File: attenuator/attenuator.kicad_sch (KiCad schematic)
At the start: 25 parts, among them J1 Conn_Coaxial, J11 Conn_02x07_Odd_Even, J2 Conn_Coaxial

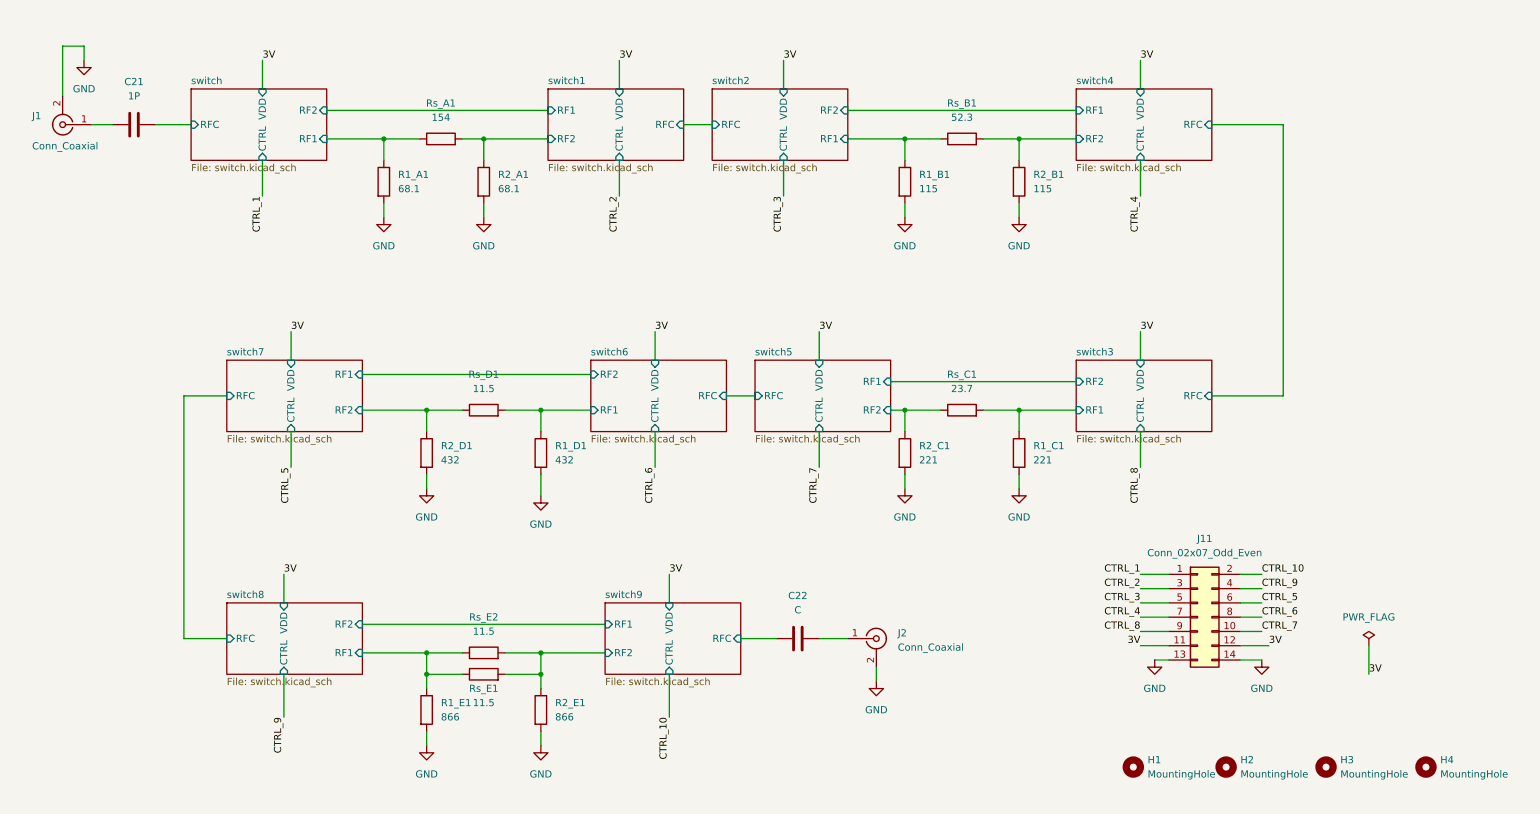
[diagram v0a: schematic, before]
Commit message: change hierarchical sheets
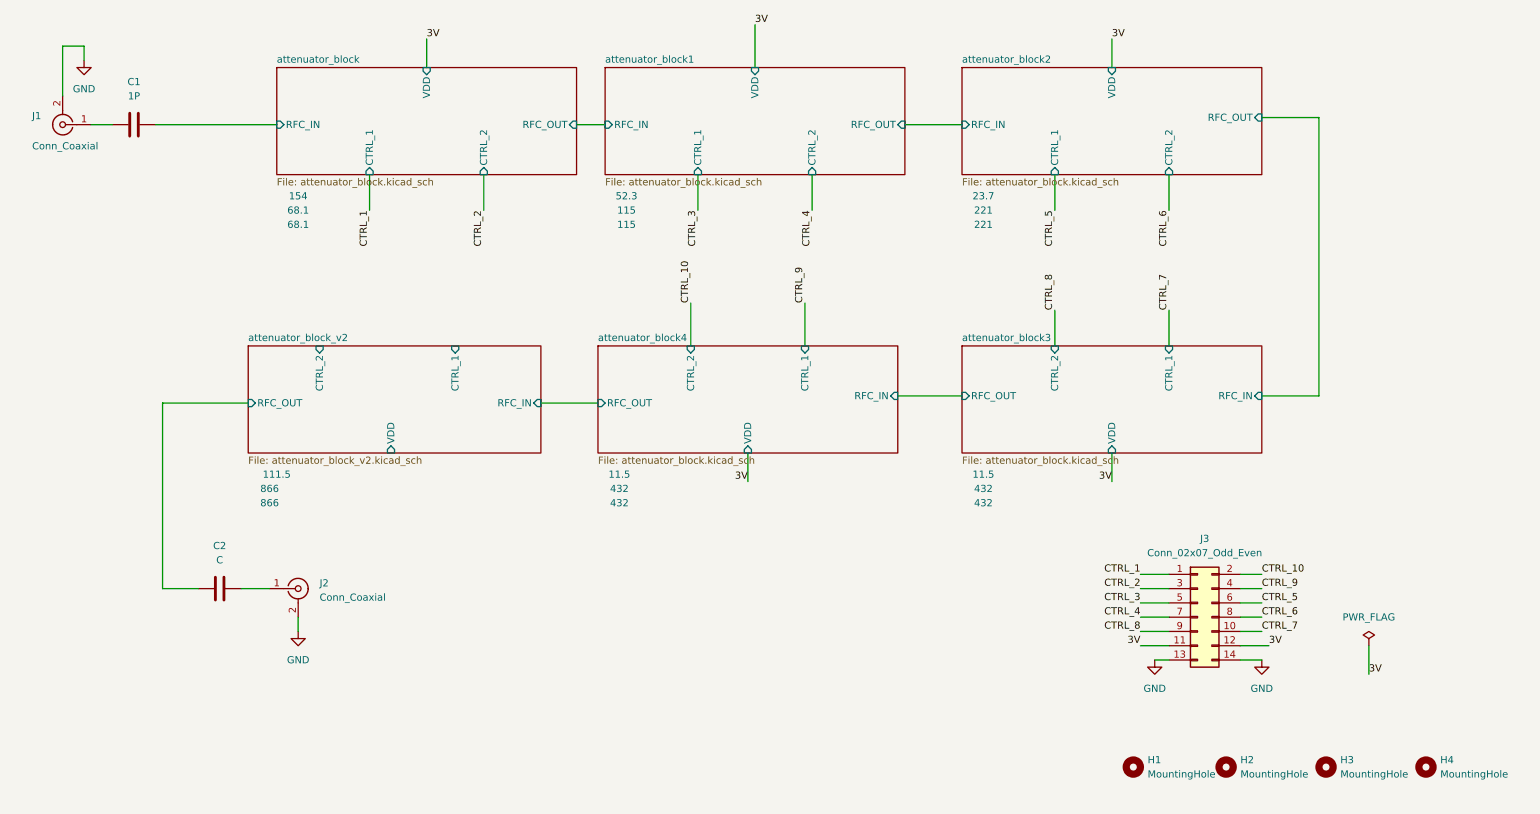
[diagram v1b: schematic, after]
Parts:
- removed R1_A1, R2_A1: 68.1, Resistor_SMD:R_0805_2012Metric_Pad1.20x1.40mm_HandSolder, symbol Device:R
- removed R1_B1, R2_B1: 115, Resistor_SMD:R_0805_2012Metric_Pad1.20x1.40mm_HandSolder, symbol Device:R
- removed R1_C1, R2_C1: 221, Resistor_SMD:R_0805_2012Metric_Pad1.20x1.40mm_HandSolder, symbol Device:R
- removed R1_D1, R2_D1: 432, Resistor_SMD:R_0805_2012Metric_Pad1.20x1.40mm_HandSolder, symbol Device:R
- removed R1_E1, R2_E1: 866, Resistor_SMD:R_0805_2012Metric_Pad1.20x1.40mm_HandSolder, symbol Device:R
- removed Rs_A1: 154, Resistor_SMD:R_0805_2012Metric_Pad1.20x1.40mm_HandSolder, symbol Device:R
- removed Rs_B1: 52.3, Resistor_SMD:R_0805_2012Metric_Pad1.20x1.40mm_HandSolder, symbol Device:R
- removed Rs_C1: 23.7, Resistor_SMD:R_0805_2012Metric_Pad1.20x1.40mm_HandSolder, symbol Device:R
- removed Rs_D1, Rs_E1, Rs_E2: 11.5, Resistor_SMD:R_0805_2012Metric_Pad1.20x1.40mm_HandSolder, symbol Device:R
- renumbered C21 to C1, C22 to C2, J11 to J3
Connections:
- net switch/RFC renamed attenuator_block/RFC_IN
- net switch9/RFC renamed attenuator_block_v2/RFC_OUT
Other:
- removed sheet switch
- removed sheet switch1
- removed sheet switch2
- removed sheet switch3
- removed sheet switch4
- removed sheet switch5
- removed sheet switch6
- removed sheet switch7
- removed sheet switch8
- removed sheet switch9
- added sheet attenuator_block (attenuator_block.kicad_sch)
- added sheet attenuator_block1 (attenuator_block.kicad_sch)
- added sheet attenuator_block2 (attenuator_block.kicad_sch)
- added sheet attenuator_block3 (attenuator_block.kicad_sch)
- added sheet attenuator_block4 (attenuator_block.kicad_sch)
- added sheet attenuator_block_v2 (attenuator_block_v2.kicad_sch)
- moved on the sheet: C2, J2

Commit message: pcb improve it
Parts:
- C1, C2: footprint Capacitor_SMD:C_0805_2012Metric -> Capacitor_SMD:C_0603_1608Metric
- J3: footprint Connector_PinHeader_2.54mm:PinHeader_2x07_P2.54mm_Vertical -> Connector_PinSocket_1.27mm:PinSocket_2x07_P1.27mm_Vertical
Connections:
- net CTRL_1: now also J3.9 (Pin_9); no longer J3.1 (Pin_1)
- net CTRL_10: now also J3.10 (Pin_10); no longer J3.2 (Pin_2)
- net CTRL_2: now also J3.7 (Pin_7); no longer J3.3 (Pin_3)
- net CTRL_4: now also J3.3 (Pin_3); no longer J3.7 (Pin_7)
- net CTRL_5: now also J3.1 (Pin_1); no longer J3.6 (Pin_6)
- net CTRL_6: now also J3.2 (Pin_2); no longer J3.8 (Pin_8)
- net CTRL_7: now also J3.4 (Pin_4); no longer J3.10 (Pin_10)
- net CTRL_8: now also J3.6 (Pin_6); no longer J3.9 (Pin_9)
- net CTRL_9: now also J3.8 (Pin_8); no longer J3.4 (Pin_4)
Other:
- removed sheet attenuator_block4
- moved on the sheet: C2, J2

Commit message: minnor changes in pcb
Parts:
- removed H1, H2, H3, H4: MountingHole, MountingHole:MountingHole_3.2mm_M3_Pad_TopBottom, symbol Mechanical:MountingHole
- added H5, H6, H7, H8: MountingHole_Pad, MountingHole:MountingHole_3.2mm_M3_Pad_TopBottom, symbol Mechanical:MountingHole_Pad
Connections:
- net GND: now also H5.1, H6.1, H7.1, H8.1
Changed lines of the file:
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@@
-    )
-  )
-  (symbol (lib_id "Mechanical:MountingHole") (at 264.16 157.48 0) (unit 1)
-    (in_bom yes) (on_board yes) (dnp no) (fields_autoplaced)
-    (property "Reference" "H4" (at 266.7 156.21 0)
-      (effects (font (size 1.27 1.27)) (justify left))
-    )
-    (property "Value" "MountingHole" (at 266.7 158.75 0)
-      (effects (font (size 1.27 1.27)) (justify left))
-    )
-    (property "Footprint" "MountingHole:MountingHole_3.2mm_M3_Pad_TopBottom" (at 264.16 157.48 0)
-      (effects (font (size 1.27 1.27)) hide)
-    )
-    (property "Datasheet" "~" (at 264.16 157.48 0)
-      (effects (font (size 1.27 1.27)) hide)
-    )
-    (instances
-      (project "attenuator"
-        (path "/3b0f5433-415e-45c9-9c4a-85a692e565e5"
-          (reference "H4") (unit 1)
-        )
-      )
     )
   )
@@
     )
   )
-  (symbol (lib_id "Mechanical:MountingHole") (at 246.38 157.48 0) (unit 1)
-    (in_bom yes) (on_board yes) (dnp no) (fields_autoplaced)
-    (property "Reference" "H3" (at 248.92 156.21 0)
-      (effects (font (size 1.27 1.27)) (justify left))
-    )
-    (property "Value" "MountingHole" (at 248.92 158.75 0)
-      (effects (font (size 1.27 1.27)) (justify left))
-    )
-    (property "Footprint" "MountingHole:MountingHole_3.2mm_M3_Pad_TopBottom" (at 246.38 157.48 0)
-      (effects (font (size 1.27 1.27)) hide)
-    )
-    (property "Datasheet" "~" (at 246.38 157.48 0)
-      (effects (font (size 1.27 1.27)) hide)
-    )
-    (instances
-      (project "attenuator"
-        (path "/3b0f5433-415e-45c9-9c4a-85a692e565e5"
-          (reference "H3") (unit 1)
-        )
-      )
-    )
-  )
   (symbol (lib_id "power:GND") (at 234.95 138.43 0) (unit 1)
     (in_bom yes) (on_board yes) (dnp no) (fields_autoplaced)
@@
         (path "/3b0f5433-415e-45c9-9c4a-85a692e565e5"
           (reference "#PWR03") (unit 1)
-        )
-      )
-    )
-  )
-  (symbol (lib_id "Mechanical:MountingHole") (at 212.09 157.48 0) (unit 1)
-    (in_bom yes) (on_board yes) (dnp no) (fields_autoplaced)
-    (property "Reference" "H1" (at 214.63 156.21 0)
-      (effects (font (size 1.27 1.27)) (justify left))
-    )
-    (property "Value" "MountingHole" (at 214.63 158.75 0)
-      (effects (font (size 1.27 1.27)) (justify left))
-    )
-    (property "Footprint" "MountingHole:MountingHole_3.2mm_M3_Pad_TopBottom" (at 212.09 157.48 0)
-      (effects (font (size 1.27 1.27)) hide)
-    )
-    (property "Datasheet" "~" (at 212.09 157.48 0)
-      (effects (font (size 1.27 1.27)) hide)
-    )
-    (instances
-      (project "attenuator"
-        (path "/3b0f5433-415e-45c9-9c4a-85a692e565e5"
-          (reference "H1") (unit 1)
         )
       )
@@
     )
   )
-  (symbol (lib_id "Mechanical:MountingHole") (at 228.6 157.48 0) (unit 1)
-    (in_bom yes) (on_board yes) (dnp no) (fields_autoplaced)
-    (property "Reference" "H2" (at 231.14 156.21 0)
-      (effects (font (size 1.27 1.27)) (justify left))
-    )
-    (property "Value" "MountingHole" (at 231.14 158.75 0)
-      (effects (font (size 1.27 1.27)) (justify left))
-    )
-    (property "Footprint" "MountingHole:MountingHole_3.2mm_M3_Pad_TopBottom" (at 228.6 157.48 0)
-      (effects (font (size 1.27 1.27)) hide)
-    )
-    (property "Datasheet" "~" (at 228.6 157.48 0)
-      (effects (font (size 1.27 1.27)) hide)
-    )
-    (instances
-      (project "attenuator"
-        (path "/3b0f5433-415e-45c9-9c4a-85a692e565e5"
-          (reference "H2") (unit 1)
+  (symbol (lib_id "Mechanical:MountingHole_Pad") (at 205.74 154.94 0) (unit 1)
+    (in_bom yes) (on_board yes) (dnp no) (fields_autoplaced)
+    (property "Reference" "H5" (at 208.28 152.4 0)
+      (effects (font (size 1.27 1.27)) (justify left))
+    )
+    (property "Value" "MountingHole_Pad" (at 208.28 154.94 0)
+      (effects (font (size 1.27 1.27)) (justify left))
+    )
+    (property "Footprint" "MountingHole:MountingHole_3.2mm_M3_Pad_TopBottom" (at 205.74 154.94 0)
+      (effects (font (size 1.27 1.27)) hide)
+    )
+    (property "Datasheet" "~" (at 205.74 154.94 0)
+      (effects (font (size 1.27 1.27)) hide)
+    )
+    (pin "1")
+    (instances
+      (project "attenuator"
+        (path "/3b0f5433-415e-45c9-9c4a-85a692e565e5"
+          (reference "H5") (unit 1)
+        )
+      )
+    )
+  )
+  (symbol (lib_id "Mechanical:MountingHole_Pad") (at 250.19 154.94 0) (unit 1)
+    (in_bom yes) (on_board yes) (dnp no) (fields_autoplaced)
+    (property "Reference" "H7" (at 252.73 152.4 0)
+      (effects (font (size 1.27 1.27)) (justify left))
+    )
+    (property "Value" "MountingHole_Pad" (at 252.73 154.94 0)
+      (effects (font (size 1.27 1.27)) (justify left))
+    )
+    (property "Footprint" "MountingHole:MountingHole_3.2mm_M3_Pad_TopBottom" (at 250.19 154.94 0)
+      (effects (font (size 1.27 1.27)) hide)
+    )
+    (property "Datasheet" "~" (at 250.19 154.94 0)
+      (effects (font (size 1.27 1.27)) hide)
+    )
+    (pin "1")
+    (instances
+      (project "attenuator"
+        (path "/3b0f5433-415e-45c9-9c4a-85a692e565e5"
+          (reference "H7") (unit 1)
+        )
+      )
+    )
+  )
+  (symbol (lib_id "power:GND") (at 205.74 157.48 0) (unit 1)
+    (in_bom yes) (on_board yes) (dnp no) (fields_autoplaced)
+    (property "Reference" "#PWR035" (at 205.74 163.83 0)
+      (effects (font (size 1.27 1.27)) hide)
+    )
+    (property "Value" "GND" (at 205.74 162.56 0)
+      (effects (font (size 1.27 1.27)))
+    )
+    (property "Footprint" "" (at 205.74 157.48 0)
+      (effects (font (size 1.27 1.27)) hide)
+    )
+    (property "Datasheet" "" (at 205.74 157.48 0)
+      (effects (font (size 1.27 1.27)) hide)
+    )
+    (pin "1")
+    (instances
+      (project "attenuator"
+        (path "/3b0f5433-415e-45c9-9c4a-85a692e565e5"
+          (reference "#PWR035") (unit 1)
+        )
+      )
+    )
+  )
+  (symbol (lib_id "Mechanical:MountingHole_Pad") (at 182.88 154.94 0) (unit 1)
+    (in_bom yes) (on_board yes) (dnp no) (fields_autoplaced)
+    (property "Reference" "H8" (at 185.42 152.4 0)
+      (effects (font (size 1.27 1.27)) (justify left))
+    )
+    (property "Value" "MountingHole_Pad" (at 185.42 154.94 0)
+      (effects (font (size 1.27 1.27)) (justify left))
+    )
+    (property "Footprint" "MountingHole:MountingHole_3.2mm_M3_Pad_TopBottom" (at 182.88 154.94 0)
+      (effects (font (size 1.27 1.27)) hide)
+    )
+    (property "Datasheet" "~" (at 182.88 154.94 0)
+      (effects (font (size 1.27 1.27)) hide)
+    )
+    (pin "1")
+    (instances
+      (project "attenuator"
+        (path "/3b0f5433-415e-45c9-9c4a-85a692e565e5"
+          (reference "H8") (unit 1)
         )
       )
@@
     )
   )
+  (symbol (lib_id "Mechanical:MountingHole_Pad") (at 228.6 154.94 0) (unit 1)
+    (in_bom yes) (on_board yes) (dnp no) (fields_autoplaced)
+    (property "Reference" "H6" (at 231.14 152.4 0)
+      (effects (font (size 1.27 1.27)) (justify left))
+    )
+    (property "Value" "MountingHole_Pad" (at 231.14 154.94 0)
+      (effects (font (size 1.27 1.27)) (justify left))
+    )
+    (property "Footprint" "MountingHole:MountingHole_3.2mm_M3_Pad_TopBottom" (at 228.6 154.94 0)
+      (effects (font (size 1.27 1.27)) hide)
+    )
+    (property "Datasheet" "~" (at 228.6 154.94 0)
+      (effects (font (size 1.27 1.27)) hide)
+    )
+    (pin "1")
+    (instances
+      (project "attenuator"
+        (path "/3b0f5433-415e-45c9-9c4a-85a692e565e5"
+          (reference "H6") (unit 1)
+        )
+      )
+    )
+  )
+  (symbol (lib_id "power:GND") (at 250.19 157.48 0) (unit 1)
+    (in_bom yes) (on_board yes) (dnp no) (fields_autoplaced)
+    (property "Reference" "#PWR037" (at 250.19 163.83 0)
+      (effects (font (size 1.27 1.27)) hide)
+    )
+    (property "Value" "GND" (at 250.19 162.56 0)
+      (effects (font (size 1.27 1.27)))
+    )
+    (property "Footprint" "" (at 250.19 157.48 0)
+      (effects (font (size 1.27 1.27)) hide)
+    )
+    (property "Datasheet" "" (at 250.19 157.48 0)
+      (effects (font (size 1.27 1.27)) hide)
+    )
+    (pin "1")
+    (instances
+      (project "attenuator"
+        (path "/3b0f5433-415e-45c9-9c4a-85a692e565e5"
+          (reference "#PWR037") (unit 1)
+        )
+      )
+    )
+  )
   (symbol (lib_id "power:PWR_FLAG") (at 254 135.89 0) (unit 1)
     (in_bom yes) (on_board yes) (dnp no) (fields_autoplaced)
@@
         )
       )
+    )
+  )
+  (symbol (lib_id "power:GND") (at 228.6 157.48 0) (unit 1)
+    (in_bom yes) (on_board yes) (dnp no) (fields_autoplaced)
+    (property "Reference" "#PWR036" (at 228.6 163.83 0)
+      (effects (font (size 1.27 1.27)) hide)
+    )
+    (property "Value" "GND" (at 228.6 162.56 0)
+      (effects (font (size 1.27 1.27)))
+    )
+    (property "Footprint" "" (at 228.6 157.48 0)
+      (effects (font (size 1.27 1.27)) hide)
+    )
+    (property "Datasheet" "" (at 228.6 157.48 0)
+      (effects (font (size 1.27 1.27)) hide)
+    )
+    (pin "1")
+    (instances
+      (project "attenuator"
+        (path "/3b0f5433-415e-45c9-9c4a-85a692e565e5"
+          (reference "#PWR036") (unit 1)
+        )
+      )
+    )
+  )
+  (symbol (lib_id "power:GND") (at 182.88 157.48 0) (unit 1)
+    (in_bom yes) (on_board yes) (dnp no) (fields_autoplaced)
+    (property "Reference" "#PWR038" (at 182.88 163.83 0)
+      (effects (font (size 1.27 1.27)) hide)
+    )
+    (property "Value" "GND" (at 182.88 162.56 0)
+      (effects (font (size 1.27 1.27)))
+    )
+    (property "Footprint" "" (at 182.88 157.48 0)
+      (effects (font (size 1.27 1.27)) hide)
+    )
+    (property "Datasheet" "" (at 182.88 157.48 0)
+      (effects (font (size 1.27 1.27)) hide)
+    )
+    (pin "1")
+    (instances
+      (project "attenuator"
+        (path "/3b0f5433-415e-45c9-9c4a-85a692e565e5"
+          (reference "#PWR038") (unit 1)
+        )
+      )
